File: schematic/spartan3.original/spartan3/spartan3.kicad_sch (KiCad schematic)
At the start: 245 parts, among them U1_clk_select_0 SPFT_Sliding_Switch-dynacore, U2 XC3S250E-4TQG144C

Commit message: FPGA pins mapping added/updated. Schematics/PCB layout :: updated according to the added/updated PINs mapping
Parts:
- removed J_CONTROL_0: Conn_01x25_Male, Connector_PinHeader_2.54mm:PinHeader_1x25_P2.54mm_Vertical, symbol Connector:Conn_01x25_Male
- added J_GND_0, J_OUT_USART1_TX_0: Conn_01x01_Male, Connector_PinHeader_2.54mm:PinHeader_1x01_P2.54mm_Vertical, symbol Connector:Conn_01x01_Male
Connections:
- net eeprom_spi_cs_n is gone; now on net P39: R_eeprom_s_0.2, U_eeprom_0.1 (S#)
- net eeprom_spi_din is gone; now on net P44: U_eeprom_0.5 (DQ0)
- net reset is gone; now on net P24: R_reset_0.2, SW_reset_0.1
- net DOUT_BUSY: now also D_out_sysbus_5.2 (A); no longer D_out_sysbus_3.2 (A)
- net GND: now also J_GND_0.1 (Pin_1)
- net HSWAP_EN: now also J_OUT_USART1_TX_0.1 (Pin_1)
- net INIT_B: now also D_out_sysbus_4.2 (A); no longer D_out_sysbus_1.2 (A)
- net P124: now also D_out_r3_r_0.2 (A)
- net P125: now also D_out_r2_r_0.2 (A); no longer D_out_r3_r_0.2 (A)
- net P126: now also D_out_r1_r_0.2 (A); no longer D_out_r2_r_0.2 (A)
- net P128: no longer D_out_r1_r_0.2 (A)
- net P129: no longer D_out_r0_r_0.2 (A)
- net P130: now also D_out_r0_r_0.2 (A); no longer D_out_bus1_0.2 (A)
- net P131: now also D_out_bus1_0.2 (A); no longer D_out_ram_r_0.2 (A)
- net P132: now also D_out_ram_r_0.2 (A); no longer D_out_acc_r_0.2 (A)
- net P134: now also D_out_acc_r_0.2 (A); no longer D_out_iar_r_0.2 (A)
- net P135: now also D_out_iar_r_0.2 (A)
- net P22: now also D_out_flags_z_0.2 (A)
- net P23: now also D_out_flags_eq_0.2 (A)
- net P25: now also D_out_flags_gt_0.2 (A)
- net P26: now also D_out_flags_C_out_0.2 (A)
- net P32: now also D_out_sysbus_0.2 (A)
- net P33: now also D_out_sysbus_1.2 (A); no longer D_out_flags_z_0.2 (A)
- net P34: now also D_out_sysbus_2.2 (A); no longer D_out_flags_eq_0.2 (A)
- net P35: now also D_out_sysbus_3.2 (A); no longer D_out_flags_gt_0.2 (A)
- net P36: no longer D_out_flags_C_out_0.2 (A)
- net P38: no longer D_out_sysbus_0.2 (A)
- net P41: no longer D_out_sysbus_2.2 (A)
- net P47: no longer D_out_sysbus_4.2 (A)
- net P48: no longer D_out_sysbus_5.2 (A)
- net P67: no longer R_in_manual_input_o_7.1, SW_in_manual_input_o_7.2 (B)
- net P69: now also R_in_manual_input_o_7.1, SW_in_manual_input_o_7.2 (B)
- net P94: now also D_out_iar_w_0.2 (A); no longer D_in_clk_manual_0.1 (K), R_in_clk_manual_0.1, SW_in_clk_manual_0.1
- net P95: now also D_in_clk_manual_0.1 (K), R_in_clk_manual_0.1, SW_in_clk_manual_0.1; no longer D_out_iar_w_0.2 (A)

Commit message: Tactile switch footprint updated. DRC rules checked/fixed
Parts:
- SW_in_acc_w_0, SW_in_bus1_0, SW_in_iar_w_0, SW_in_ir_w_0, SW_in_is_bus1_w_0, SW_in_r0_w_0, SW_in_r1_w_0, SW_in_r2_w_0, SW_in_r3_w_0, SW_in_ram_a_w_0, SW_in_ram_w_0, SW_in_read_reg_en_0, SW_in_temp_w_0, SW_in_write_reg_en_0, SW_pwr_0: footprint Button_Switch_THT:SW_Push_2P2T_Toggle_CK_PVA2OAH5xxxxxxV2 -> SW_SPDT_small:Tactile_6PIN_SPDT_8.5x8.5mm

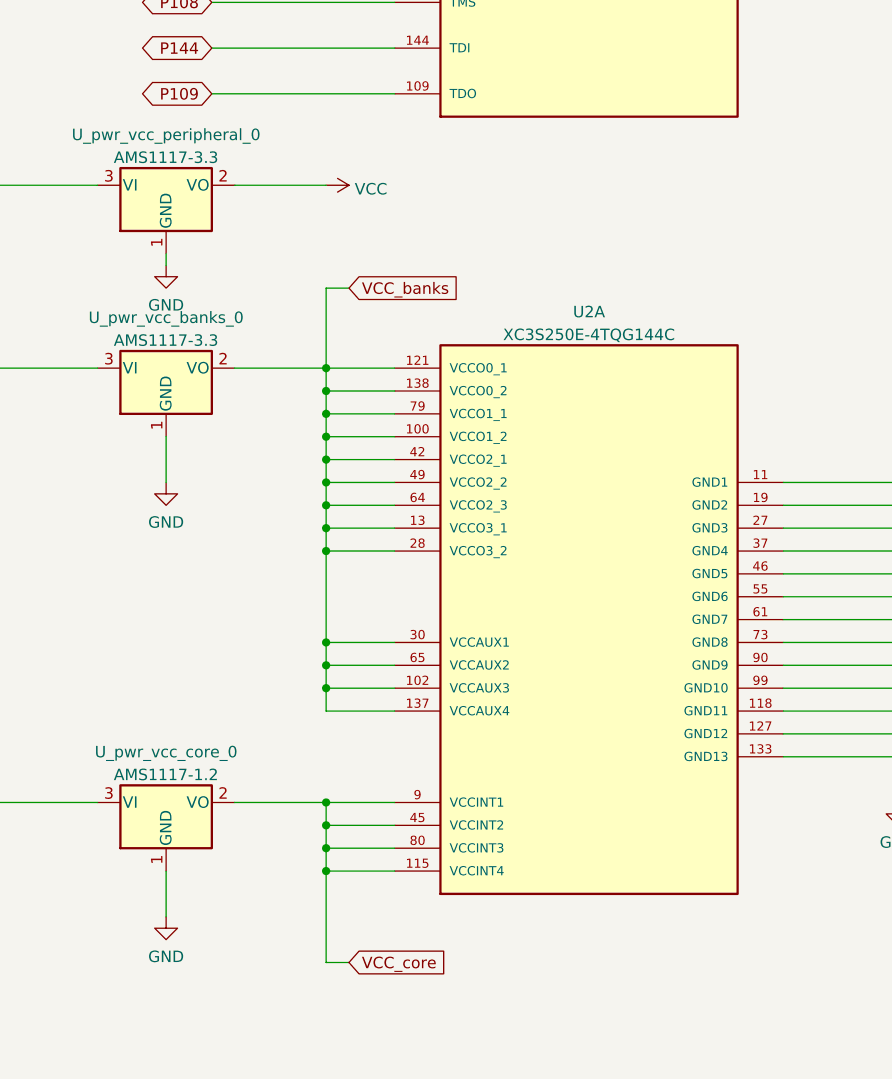
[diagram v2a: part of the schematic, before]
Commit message: Schematics :: power capicators added. PCB layout :: labels updated
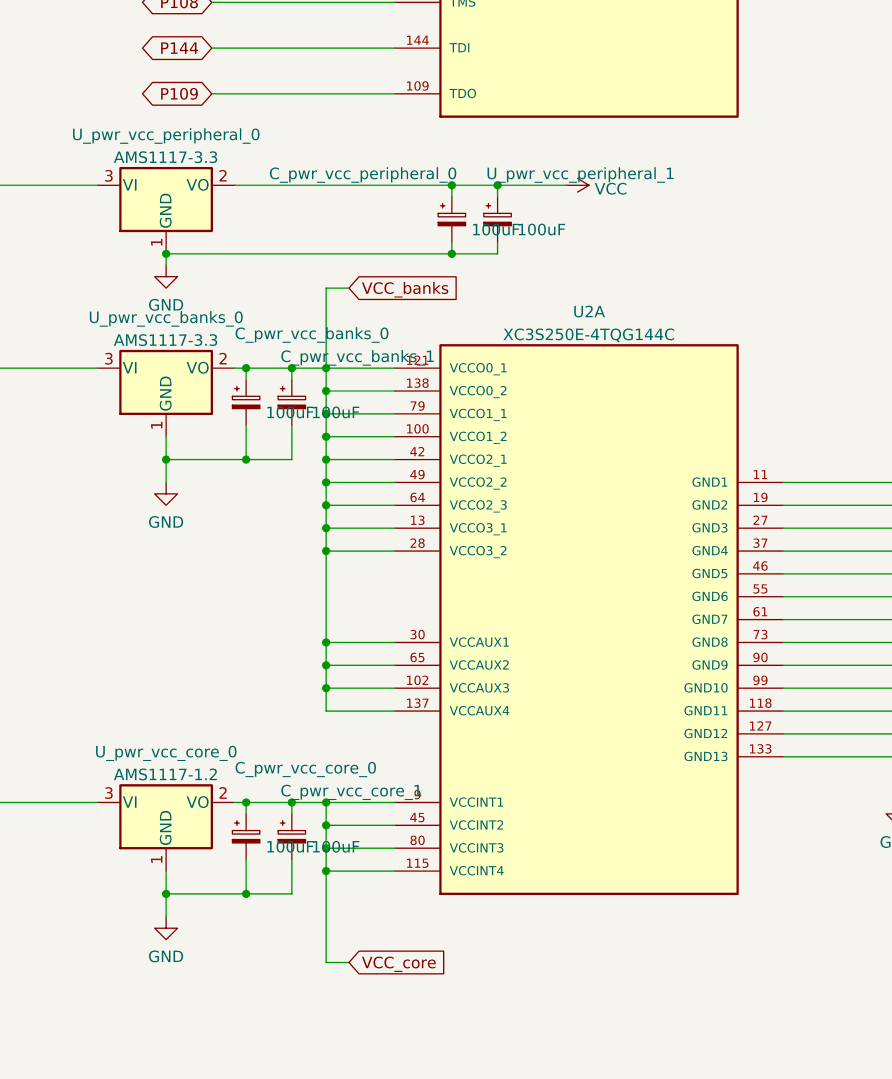
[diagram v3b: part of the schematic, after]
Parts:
- added C_pwr_vcc_banks_0, C_pwr_vcc_banks_1, C_pwr_vcc_core_0, C_pwr_vcc_core_1, C_pwr_vcc_peripheral_0, U_pwr_vcc_peripheral_1: 100uF, Capacitor_SMD:CP_Elec_6.3x5.4, symbol Device:C_Polarized_Small
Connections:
- net GND: now also C_pwr_vcc_banks_0.2, C_pwr_vcc_banks_1.2, C_pwr_vcc_core_0.2, C_pwr_vcc_core_1.2, C_pwr_vcc_peripheral_0.2, U_pwr_vcc_peripheral_1.2
- net VCC: now also C_pwr_vcc_peripheral_0.1, U_pwr_vcc_peripheral_1.1
- net VCC_banks: now also C_pwr_vcc_banks_0.1, C_pwr_vcc_banks_1.1
- net VCC_core: now also C_pwr_vcc_core_0.1, C_pwr_vcc_core_1.1

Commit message: Schematics/PCB layout :: Oscilator updated, helpful PINs extracted
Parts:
- removed X_clk_0: SG-51, Oscillator:Oscillator_SeikoEpson_SG-8002DB, symbol Oscillator:SG-51
- added J_D0_DIN_0, J_DONE_0, J_DOUT_BUSY_0, J_INIT_B_0, J_M0_0, J_M1_0, J_M2_0, J_P101_0, J_P107_0, J_P111_0, J_P114_0, J_P128_0, J_P129_0, J_P29_0, J_P31_0, J_P36_0, J_P38_0, J_P47_0, J_P48_0, J_P67_0, J_P68_0, J_P70_0, J_P78_0, J_P84_0, J_PROG_B_0, J_TCK_0, J_TDI_0, J_TDO_0, J_TMS_0, J_VCC_0, J_VCC_banks_0, J_VCC_core_0, J_eeprom_spi_clk_0, J_eeprom_spi_cs_n_0, J_eeprom_spi_din_0: Conn_01x01_Male, Connector_Wire:SolderWirePad_1x01_SMD_1x2mm, symbol Connector:Conn_01x01_Male
- added J_clk_0: Conn_01x01_Male, Connector_PinHeader_2.54mm:PinHeader_1x01_P2.54mm_Vertical, symbol Connector:Conn_01x01_Male
- added X_clk_0: XO91, Oscillator:Oscillator_SMD_EuroQuartz_XO91-4Pin_7.0x5.0mm_HandSoldering, symbol Oscillator:XO91
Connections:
- net CCLK: now also J_eeprom_spi_clk_0.1 (Pin_1)
- net D0_DIN: now also J_D0_DIN_0.1 (Pin_1)
- net DONE: now also J_DONE_0.1 (Pin_1)
- net DOUT_BUSY: now also J_DOUT_BUSY_0.1 (Pin_1)
- net GND: now also X_clk_0.2 (GND)
- net INIT_B: now also J_INIT_B_0.1 (Pin_1)
- net M0: now also J_M0_0.1 (Pin_1)
- net M1: now also J_M1_0.1 (Pin_1)
- net M2: now also J_M2_0.1 (Pin_1)
- net P1: now also J_PROG_B_0.1 (Pin_1)
- net P101: now also J_P101_0.1 (Pin_1)
- net P107: now also J_P107_0.1 (Pin_1)
- net P108: now also J_TMS_0.1 (Pin_1)
- net P109: now also J_TDO_0.1 (Pin_1)
- net P110: now also J_TCK_0.1 (Pin_1)
- net P111: now also J_P111_0.1 (Pin_1)
- net P114: now also J_P114_0.1 (Pin_1)
- net P128: now also J_P128_0.1 (Pin_1)
- net P129: now also J_P129_0.1 (Pin_1)
- net P144: now also J_TDI_0.1 (Pin_1)
- net P29: now also J_P29_0.1 (Pin_1)
- net P31: now also J_P31_0.1 (Pin_1)
- net P36: now also J_P36_0.1 (Pin_1)
- net P38: now also J_P38_0.1 (Pin_1)
- net P39: now also J_eeprom_spi_cs_n_0.1 (Pin_1)
- net P44: now also J_eeprom_spi_din_0.1 (Pin_1)
- net P47: now also J_P47_0.1 (Pin_1)
- net P48: now also J_P48_0.1 (Pin_1)
- net P56: now also J_clk_0.1 (Pin_1)
- net P67: now also J_P67_0.1 (Pin_1)
- net P68: now also J_P68_0.1 (Pin_1)
- net P70: now also J_P70_0.1 (Pin_1)
- net P78: now also J_P78_0.1 (Pin_1)
- net P84: now also J_P84_0.1 (Pin_1)
- net VCC: now also J_VCC_0.1 (Pin_1)
- net VCC_banks: now also J_VCC_banks_0.1 (Pin_1)
- net VCC_core: now also J_VCC_core_0.1 (Pin_1)
- net at C_clk_0.1, C_clk_1.1, L_clk_0.2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: now also X_clk_0.4 (V+)
- net at R_clk_out_0.1: now also X_clk_0.3 (OUT)
- net at R_clk_oe_0.2: now also X_clk_0.1 (EN)

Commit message: Schematics/PCB layout/FPGA pin mapping updated. Gerber/Drill files generated
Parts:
- removed C_pwr_vcc_banks_0, C_pwr_vcc_banks_1: 100uF, Capacitor_SMD:CP_Elec_6.3x5.4, symbol Device:C_Polarized_Small
- removed J_M0_0, J_M1_0, J_M2_0, J_P38_0, J_P47_0, J_P67_0, J_P68_0, J_P70_0, J_VCC_banks_0: Conn_01x01_Male, Connector_Wire:SolderWirePad_1x01_SMD_1x2mm, symbol Connector:Conn_01x01_Male
- removed L_clk_0: L_Small, Inductor_SMD:L_0805_2012Metric_Pad1.05x1.20mm_HandSolder, symbol Device:L_Small
- removed U_pwr_vcc_banks_0: AMS1117-3.3, Package_TO_SOT_SMD:SOT-223-3_TabPin2, symbol Regulator_Linear:AMS1117-3.3
- added C_clk_out_0: 15pF, Capacitor_SMD:C_0805_2012Metric_Pad1.18x1.45mm_HandSolder, symbol Device:C_Small
- added C_pwr_aux_0, C_pwr_aux_1: 100uF, Capacitor_SMD:CP_Elec_6.3x5.4, symbol Device:C_Polarized_Small
- added J_VCC_aux_0: Conn_01x01_Male, Connector_Wire:SolderWirePad_1x01_SMD_1x2mm, symbol Connector:Conn_01x01_Male
- added R_HSWAP_EN_0, R_M_0, R_VS_0, R_VS_1, R_VS_2: 10K, Resistor_SMD:R_0805_2012Metric_Pad1.20x1.40mm_HandSolder, symbol Device:R_US
- added R_eeprom_spi_clk_pulldown_0, R_eeprom_spi_clk_pullup_0: 100R, Resistor_SMD:R_0805_2012Metric_Pad1.20x1.40mm_HandSolder, symbol Device:R_US
- added U_pwr_aux_0: AMS1117-2.5, Package_TO_SOT_SMD:SOT-223-3_TabPin2, symbol Regulator_Linear:AMS1117-2.5
- D_in_acc_r_0, D_in_bus1_one_0, D_in_bus1_ps_0, D_in_iar_r_0, D_in_ir_r_0, D_in_is_clk_external_0, D_in_is_clk_high_0, D_in_is_clk_low_0, D_in_is_clk_manual_0, D_in_is_clk_veryhigh_0, D_in_manual_input_r_0, D_in_none_r_0, D_in_r0_r_0, D_in_r1_r_0, D_in_r2_r_0, D_in_r3_r_0, D_in_ram_r_0, D_out_acc_r_0, D_out_bus1_0, D_out_can_read_0, D_out_can_write_0, D_out_clkr_0, D_out_flags_eq_0, D_out_iar_r_0, D_out_is_bus1_w_0, D_out_r0_r_0, D_out_r1_r_0, D_out_r2_r_0, D_out_r3_r_0, D_out_ram_r_0, D_vcc_0: value LED_Small -> LED green 2.0V/20mA
- D_in_acc_w_0, D_in_iar_w_0, D_in_ir_w_0, D_in_is_bus1_w_0, D_in_r0_w_0, D_in_r1_w_0, D_in_r2_w_0, D_in_r3_w_0, D_in_ram_a_w_0, D_in_ram_w_0, D_in_read_reg_en_0, D_in_temp_w_0, D_in_write_reg_en_0, D_out_acc_w_0, D_out_clkw_0, D_out_flags_C_out_0, D_out_flags_w_0, D_out_iar_w_0, D_out_ir_w_0, D_out_r0_w_0, D_out_r1_w_0, D_out_r2_w_0, D_out_r3_w_0, D_out_ram_a_w_0, D_out_ram_w_0, D_out_sysbus_0, D_out_sysbus_1, D_out_sysbus_2, D_out_sysbus_3, D_out_sysbus_4, D_out_sysbus_5, D_out_sysbus_6, D_out_sysbus_7, D_out_temp_w_0: value LED_Small -> LED red 2.0V/20mA
- D_in_clk_manual_0, D_out_clk_internal_0, D_out_clkc_0, D_out_flags_gt_0: value LED_Small -> LED yellow 2.0V/20mA
- D_out_flags_z_0: value LED_Small -> LED blue 2.0V/20mA
- D_out_s1_0, D_out_s2_0, D_out_s3_0, D_out_s4_0, D_out_s5_0, D_out_s6_0: value LED_Small -> LED orange 2.0V/20mA
- F_pwr_0: value Fuse_Small -> Fuse 3.3V / 2A
- R_clk_oe_0: value 10K -> 1K
- renumbered C_pwr_vcc_peripheral_0 to C_pwr_vcc_0, U_pwr_vcc_peripheral_0 to U_pwr_vcc_0, U_pwr_vcc_peripheral_1 to U_pwr_vcc_1
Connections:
- net CCLK: now also R_eeprom_spi_clk_pulldown_0.1, R_eeprom_spi_clk_pullup_0.1
- net GND: now also J_FPGA_B_2.21 (Pin_21), J_FPGA_B_2.24 (Pin_24), U2.57 (M2), U2.60 (M1), C_clk_out_0.2, C_pwr_aux_0.2, C_pwr_aux_1.2, R_eeprom_spi_clk_pulldown_0.2, U_pwr_aux_0.1 (GND)
- net HSWAP_EN: now also R_HSWAP_EN_0.1; no longer J_OUT_USART1_TX_0.1 (Pin_1)
- net M0: now also R_M_0.1; no longer R_in_manual_input_o_5.1, SW_in_manual_input_o_5.2 (B)
- net P38: now also R_in_manual_input_o_0.1, SW_in_manual_input_o_0.2 (B)
- net P41: now also R_in_manual_input_o_1.1, SW_in_manual_input_o_1.2 (B)
- net P47: now also R_in_manual_input_o_2.1, SW_in_manual_input_o_2.2 (B)
- net P52: now also J_OUT_USART1_TX_0.1 (Pin_1)
- net P54: now also R_in_manual_input_o_3.1, SW_in_manual_input_o_3.2 (B); no longer R_in_manual_input_o_0.1, SW_in_manual_input_o_0.2 (B)
- net P58: now also R_in_manual_input_o_4.1, SW_in_manual_input_o_4.2 (B); no longer R_in_manual_input_o_2.1, SW_in_manual_input_o_2.2 (B)
- net P59: now also R_in_manual_input_o_5.1, SW_in_manual_input_o_5.2 (B); no longer R_in_manual_input_o_3.1, SW_in_manual_input_o_3.2 (B)
- net P67: now also R_VS_2.1
- net P68: now also R_VS_1.1
- net P70: now also R_VS_0.1
- net VCC: now also C_clk_0.1, C_clk_1.1, C_eeprom_vcc_0.2, J_FPGA_B_0.13 (Pin_13), J_FPGA_B_1.28 (Pin_28), J_FPGA_B_1.30 (Pin_30), J_FPGA_B_1.7 (Pin_7), J_FPGA_B_2.13 (Pin_13), J_FPGA_B_2.28 (Pin_28), J_FPGA_B_2.29 (Pin_29), J_FPGA_B_2.6 (Pin_6), J_FPGA_B_3.13 (Pin_13), J_FPGA_B_3.28 (Pin_28), J_FPGA_B_3.30 (Pin_30), R_clk_oe_0.1, R_eeprom_hold_0.2, R_eeprom_s_0.1, R_eeprom_w_0.1, U2.100 (VCCO1_2), U2.121 (VCCO0_1), U2.13 (VCCO3_1), U2.138 (VCCO0_2), U2.28 (VCCO3_2), U2.42 (VCCO2_1), U2.49 (VCCO2_2), U2.64 (VCCO2_3), U2.79 (VCCO1_1), U_eeprom_0.8 (Vcc), X_clk_0.4 (V+), R_HSWAP_EN_0.2, R_M_0.2, R_VS_0.2, R_VS_1.2, R_VS_2.2, R_eeprom_spi_clk_pullup_0.2
- net at R_clk_out_0.1, X_clk_0.3 (OUT): now also C_clk_out_0.1
- net at SW_pwr_0.2 (B), U_pwr_vcc_0.3 (VI), U_pwr_vcc_core_0.3 (VI): now also U_pwr_aux_0.3 (VI)
- removed net M1: J_FPGA_B_2.24 (Pin_24), R_in_manual_input_o_4.1, SW_in_manual_input_o_4.2 (B), U2.60 (M1)
- removed net M2: J_FPGA_B_2.21 (Pin_21), R_in_manual_input_o_1.1, SW_in_manual_input_o_1.2 (B), U2.57 (M2)
- removed net VCC_banks: C_eeprom_vcc_0.2, J_FPGA_B_0.13 (Pin_13), J_FPGA_B_1.28 (Pin_28), J_FPGA_B_1.30 (Pin_30), J_FPGA_B_1.7 (Pin_7), J_FPGA_B_2.13 (Pin_13), J_FPGA_B_2.28 (Pin_28), J_FPGA_B_2.29 (Pin_29), J_FPGA_B_2.6 (Pin_6), J_FPGA_B_3.13 (Pin_13), J_FPGA_B_3.28 (Pin_28), J_FPGA_B_3.30 (Pin_30), P_JTAG_0.2 (VCC_ref), R_eeprom_hold_0.2, R_eeprom_s_0.1, R_eeprom_w_0.1, U2.100 (VCCO1_2), U2.102 (VCCAUX3), U2.121 (VCCO0_1), U2.13 (VCCO3_1), U2.137 (VCCAUX4), U2.138 (VCCO0_2), U2.28 (VCCO3_2), U2.30 (VCCAUX1), U2.42 (VCCO2_1), U2.49 (VCCO2_2), U2.64 (VCCO2_3), U2.65 (VCCAUX2), U2.79 (VCCO1_1), U_eeprom_0.8 (Vcc)
- new net VCC_aux: C_pwr_aux_0.1, C_pwr_aux_1.1, J_VCC_aux_0.1 (Pin_1), P_JTAG_0.2 (VCC_ref), U2.102 (VCCAUX3), U2.137 (VCCAUX4), U2.30 (VCCAUX1), U2.65 (VCCAUX2), U_pwr_aux_0.2 (VO)
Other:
- note added: "CPU Control"
